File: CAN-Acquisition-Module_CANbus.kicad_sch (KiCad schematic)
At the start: 20 parts, among them J5 OSTVN04A150, J6 OSTVN04A150, U5 SN65HVD235

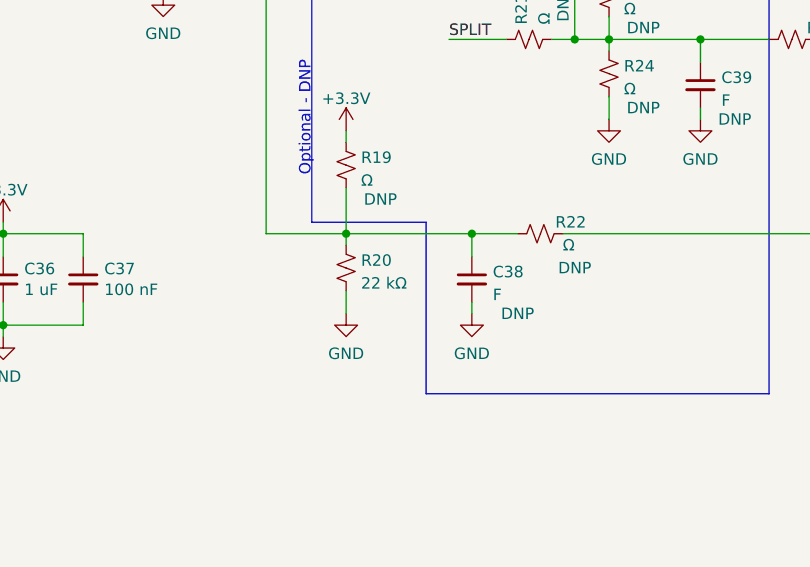
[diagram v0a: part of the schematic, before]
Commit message: Created Rev B1
Replaced buck regulator S-8581AA with AP63200 because of shortage
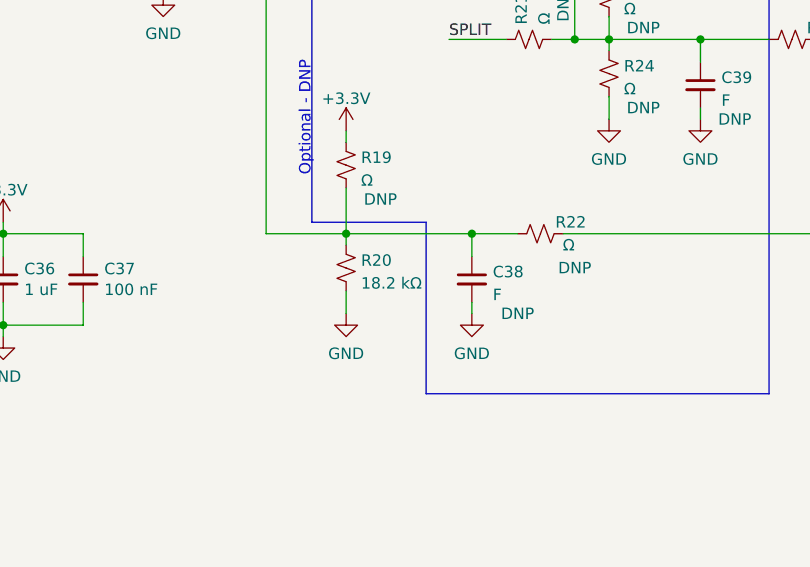
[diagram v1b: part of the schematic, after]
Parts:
- C33, C38, C39, R17, R18, R19, R21, R22, R23, R24: LCSC DNP -> (none); LCSC P/N (none) -> DNP; LCSC Package (none) -> DNP; LCSC Specs (none) -> DNP
- C34, C35: LCSC P/N (none) -> C126580; LCSC Package (none) -> 0603; LCSC Specs (none) -> 47pF NP0/C0G 50V
- C36: LCSC P/N (none) -> C386079; LCSC Package (none) -> 0603; LCSC Specs (none) -> 1uF X7R 25V
- C37: LCSC P/N (none) -> C77014; LCSC Package (none) -> 0402; LCSC Specs (none) -> 100nF X7R 16V
- D10: LCSC C284078 -> (none); LCSC P/N (none) -> C284078; LCSC Package (none) -> SOT-23; LCSC Specs (none) -> PESD2CAN
- J5, J6: LCSC C708735 -> (none); LCSC P/N (none) -> C708735; LCSC Package (none) -> 1x4 P=2.54mm; LCSC Specs (none) -> DG308-2.54-04P-14-00A(H)
- R20: value 22 kΩ -> 18.2 kΩ; LCSC P/N (none) -> C22892; LCSC Package (none) -> 0603; LCSC Specs (none) -> 18K2 1%; Mfr. Stackpole -> (none); P/N RMCF0603FT22K0 -> (none)
- R25: LCSC P/N (none) -> C22548; LCSC Package (none) -> 0603; LCSC Specs (none) -> 1K 1%
- U5: LCSC C111810 -> (none); LCSC P/N (none) -> C111810; LCSC Package (none) -> SOIC-8; LCSC Specs (none) -> SN65HVD235
